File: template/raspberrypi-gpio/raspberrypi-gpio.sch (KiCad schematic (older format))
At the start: 1 part, among them P1 CONN_13X2

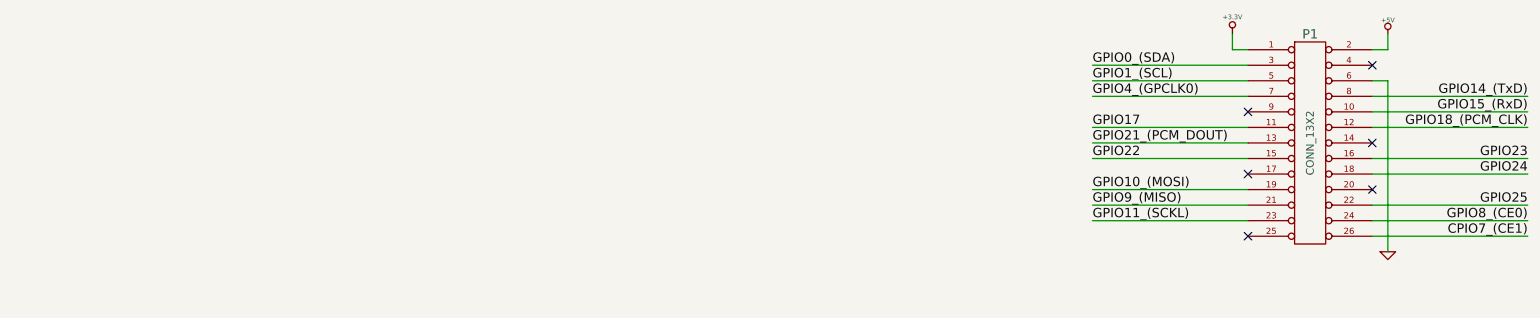
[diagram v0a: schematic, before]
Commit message: switch a template's board format to kicad_pcb format
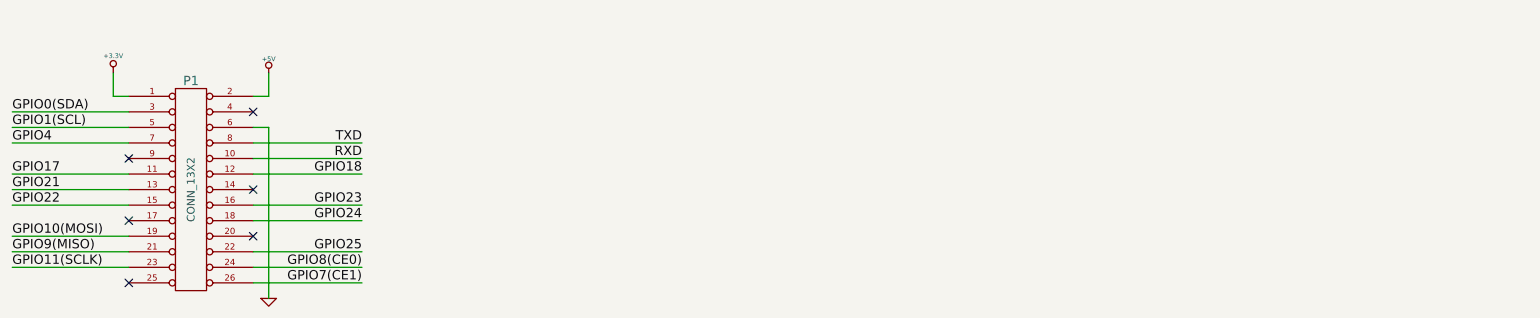
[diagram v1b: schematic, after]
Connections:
- net CPIO7_(CE1) renamed GPIO7(CE1)
- net GPIO0_(SDA) renamed GPIO0(SDA)
- net GPIO10_(MOSI) renamed GPIO10(MOSI)
- net GPIO11_(SCKL) renamed GPIO11(SCLK)
- net GPIO14_(TxD) renamed TXD
- net GPIO15_(RxD) renamed RXD
- net GPIO18_(PCM_CLK) renamed GPIO18
- net GPIO1_(SCL) renamed GPIO1(SCL)
- net GPIO21_(PCM_DOUT) renamed GPIO21
- net GPIO4_(GPCLK0) renamed GPIO4
- net GPIO8_(CE0) renamed GPIO8(CE0)
- net GPIO9_(MISO) renamed GPIO9(MISO)
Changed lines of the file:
@@
-EESchema Schematic File Version 2  date 03/08/2012 23:04:32
+EESchema Schematic File Version 2  date 15/11/2012 21:22:43
 LIBS:power
 LIBS:device
@@
 LIBS:contrib
 LIBS:valves
-EELAYER 43  0
+LIBS:rpi-cache
+EELAYER 27 0
 EELAYER END
 $Descr A4 11693 8268
@@
 Sheet 1 1
 Title ""
-Date "3 aug 2012"
+Date "15 nov 2012"
 Rev ""
 Comp ""
@@
 $Comp
 L CONN_13X2 P1
-U 1 1 501C45CC
-P 9600 1500
-F 0 "P1" H 9600 2200 60  0000 C CNN
-F 1 "CONN_13X2" V 9600 1500 50  0000 C CNN
-	1    9600 1500
+U 1 1 50A55ABA
+P 2400 1800
+F 0 "P1" H 2400 2500 60  0000 C CNN
+F 1 "CONN_13X2" V 2400 1800 50  0000 C CNN
+	1    2400 1800
 	1    0    0    -1
 $EndComp
 $Comp
-L +5V #PWR01
-U 1 1 501C4637
-P 10100 800
-F 0 "#PWR01" H 10100 890 20  0001 C CNN
-F 1 "+5V" H 10100 890 30  0000 C CNN
-	1    10100 800
-	1    0    0    -1
-$EndComp
-$Comp
-L +3.3V #PWR02
-U 1 1 501C4646
-P 9100 800
-F 0 "#PWR02" H 9100 760 30  0001 C CNN
-F 1 "+3.3V" H 9100 910 30  0000 C CNN
-	1    9100 800
-	1    0    0    -1
-$EndComp
-$Comp
-L GND #PWR03
-U 1 1 501C4659
-P 10100 2200
-F 0 "#PWR03" H 10100 2200 30  0001 C CNN
-F 1 "GND" H 10100 2130 30  0001 C CNN
-	1    10100 2200
+L +3.3V #PWR01
+U 1 1 50A55B18
+P 1900 1050
+F 0 "#PWR01" H 1900 1010 30  0001 C CNN
+F 1 "+3.3V" H 1900 1160 30  0000 C CNN
+	1    1900 1050
 	1    0    0    -1
 $EndComp
 Wire Wire Line
-	10000 1100 10100 1100
+	1900 1050 1900 1200
 Wire Wire Line
-	10100 1100 10100 2200
+	1900 1200 2000 1200
+$Comp
+L +5V #PWR02
+U 1 1 50A55B2E
+P 2900 1050
+F 0 "#PWR02" H 2900 1140 20  0001 C CNN
+F 1 "+5V" H 2900 1140 30  0000 C CNN
+	1    2900 1050
+	1    0    0    -1
+$EndComp
 Wire Wire Line
-	10000 900  10100 900
+	2900 1050 2900 1200
 Wire Wire Line
-	10100 900  10100 800
+	2900 1200 2800 1200
+NoConn ~ 2800 1300
 Wire Wire Line
-	9200 900  9100 900
+	2000 1300 1250 1300
 Wire Wire Line
-	9100 900  9100 800
+	2000 1400 1250 1400
+Text Label 1250 1300 0    60   ~ 0
+GPIO0(SDA)
+Text Label 1250 1400 0    60   ~ 0
+GPIO1(SCL)
 Wire Wire Line
-	10000 1200 11000 1200
+	2000 1500 1250 1500
+Text Label 1250 1500 0    60   ~ 0
+GPIO4
+NoConn ~ 2000 1600
 Wire Wire Line
-	10000 1300 11000 1300
-Text Label 11000 1200 2    60   ~ 0
-GPIO14_(TxD)
-Text Label 11000 1300 2    60   ~ 0
-GPIO15_(RxD)
+	2000 1700 1250 1700
 Wire Wire Line
-	10000 1400 11000 1400
-Text Label 11000 1400 2    60   ~ 0
-GPIO18_(PCM_CLK)
+	2000 1800 1250 1800
 Wire Wire Line
-	10000 1600 11000 1600
+	2000 1900 1250 1900
+Text Label 1250 1700 0    60   ~ 0
+GPIO17
+Text Label 1250 1800 0    60   ~ 0
+GPIO21
+Text Label 1250 1900 0    60   ~ 0
+GPIO22
+NoConn ~ 2000 2000
 Wire Wire Line
-	10000 1700 11000 1700
-Text Label 11000 1600 2    60   ~ 0
+	2000 2100 1250 2100
+Wire Wire Line
+	2000 2200 1250 2200
+Wire Wire Line
+	2000 2300 1250 2300
+Text Label 1250 2100 0    60   ~ 0
+GPIO10(MOSI)
+Text Label 1250 2200 0    60   ~ 0
+GPIO9(MISO)
+Text Label 1250 2300 0    60   ~ 0
+GPIO11(SCLK)
+NoConn ~ 2000 2400
+$Comp
+L GND #PWR03
+U 1 1 50A55C3F
+P 2900 2500
+F 0 "#PWR03" H 2900 2500 30  0001 C CNN
+F 1 "GND" H 2900 2430 30  0001 C CNN
+	1    2900 2500
+	1    0    0    -1
+$EndComp
+Wire Wire Line
+	2900 2500 2900 1400
+Wire Wire Line
+	2900 1400 2800 1400
+Wire Wire Line
+	2800 1500 3500 1500
+Wire Wire Line
+	2800 1600 3500 1600
+Text Label 3500 1500 2    60   ~ 0
+TXD
+Text Label 3500 1600 2    60   ~ 0
+RXD
+Wire Wire Line
+	2800 1700 3500 1700
+Text Label 3500 1700 2    60   ~ 0
+GPIO18
+NoConn ~ 2800 1800
+Wire Wire Line
+	2800 1900 3500 1900
+Wire Wire Line
+	2800 2000 3500 2000
+Text Label 3500 1900 2    60   ~ 0
 GPIO23
-Text Label 11000 1700 2    60   ~ 0
+Text Label 3500 2000 2    60   ~ 0
 GPIO24
+NoConn ~ 2800 2100
 Wire Wire Line
-	10000 1900 11000 1900
+	2800 2200 3500 2200
+Text Label 3500 2200 2    60   ~ 0
+GPIO25
 Wire Wire Line
-	10000 2000 11000 2000
+	2800 2300 3500 2300
 Wire Wire Line
-	10000 2100 11000 2100
-Text Label 11000 1900 2    60   ~ 0
-GPIO25
-Text Label 11000 2000 2    60   ~ 0
-GPIO8_(CE0)
-Text Label 11000 2100 2    60   ~ 0
-CPIO7_(CE1)
-NoConn ~ 10000 1800
-NoConn ~ 10000 1500
-NoConn ~ 10000 1000
-Wire Wire Line
-	9200 1000 8200 1000
-Wire Wire Line
-	9200 1100 8200 1100
-Wire Wire Line
-	9200 1200 8200 1200
-Wire Wire Line
-	9200 1400 8200 1400
-Wire Wire Line
-	9200 1500 8200 1500
-Wire Wire Line
-	9200 1600 8200 1600
-Wire Wire Line
-	9200 1800 8200 1800
-Wire Wire Line
-	9200 1900 8200 1900
-Wire Wire Line
-	9200 2000 8200 2000
-NoConn ~ 9200 2100
-NoConn ~ 9200 1700
-NoConn ~ 9200 1300
-Text Label 8200 1000 0    60   ~ 0
-GPIO0_(SDA)
-Text Label 8200 1100 0    60   ~ 0
-GPIO1_(SCL)
-Text Label 8200 1200 0    60   ~ 0
-GPIO4_(GPCLK0)
-Text Label 8200 1400 0    60   ~ 0
-GPIO17
-Text Label 8200 1500 0    60   ~ 0
-GPIO21_(PCM_DOUT)
-Text Label 8200 1600 0    60   ~ 0
-GPIO22
-Text Label 8200 1800 0    60   ~ 0
-GPIO10_(MOSI)
-Text Label 8200 1900 0    60   ~ 0
-GPIO9_(MISO)
-Text Label 8200 2000 0    60   ~ 0
-GPIO11_(SCKL)
+	2800 2400 3500 2400
+Text Label 3500 2300 2    60   ~ 0
+GPIO8(CE0)
+Text Label 3500 2400 2    60   ~ 0
+GPIO7(CE1)
 $EndSCHEMATC
